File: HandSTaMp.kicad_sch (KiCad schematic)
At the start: 19 parts, among them J1 USB_C_Receptacle_USB2.0_16P, J2 SDI, J3 Pins, J4 ⏚, SW1 Row 0, Col+0, SW2 Row 0, Col+1, U2 PRTR5V0U2X, U4 CH32X035G8U6

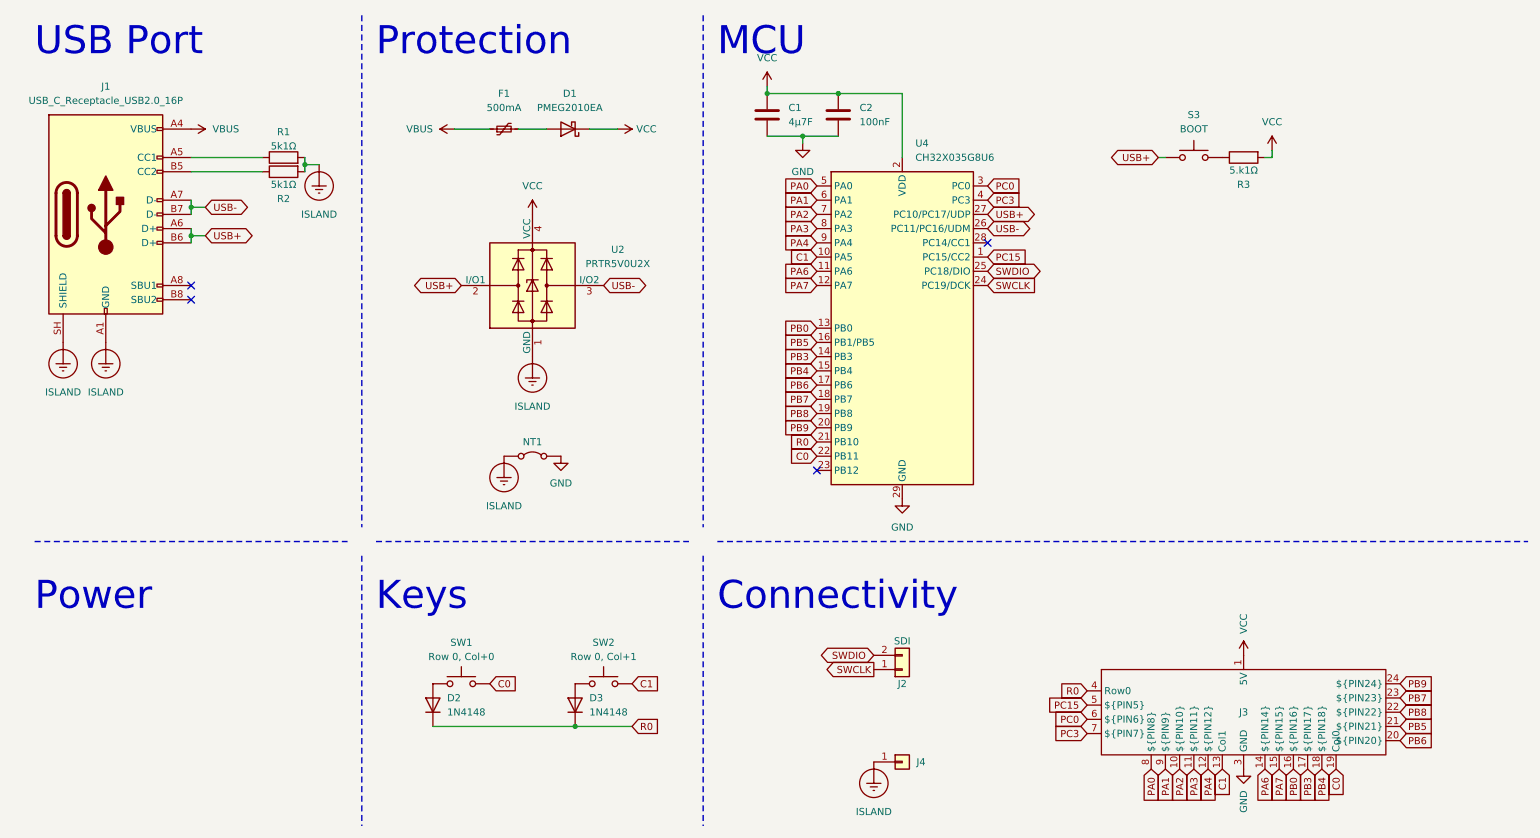
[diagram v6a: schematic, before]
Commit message: Draft equal number of extra corner pins on each side
Pins need relabelling!
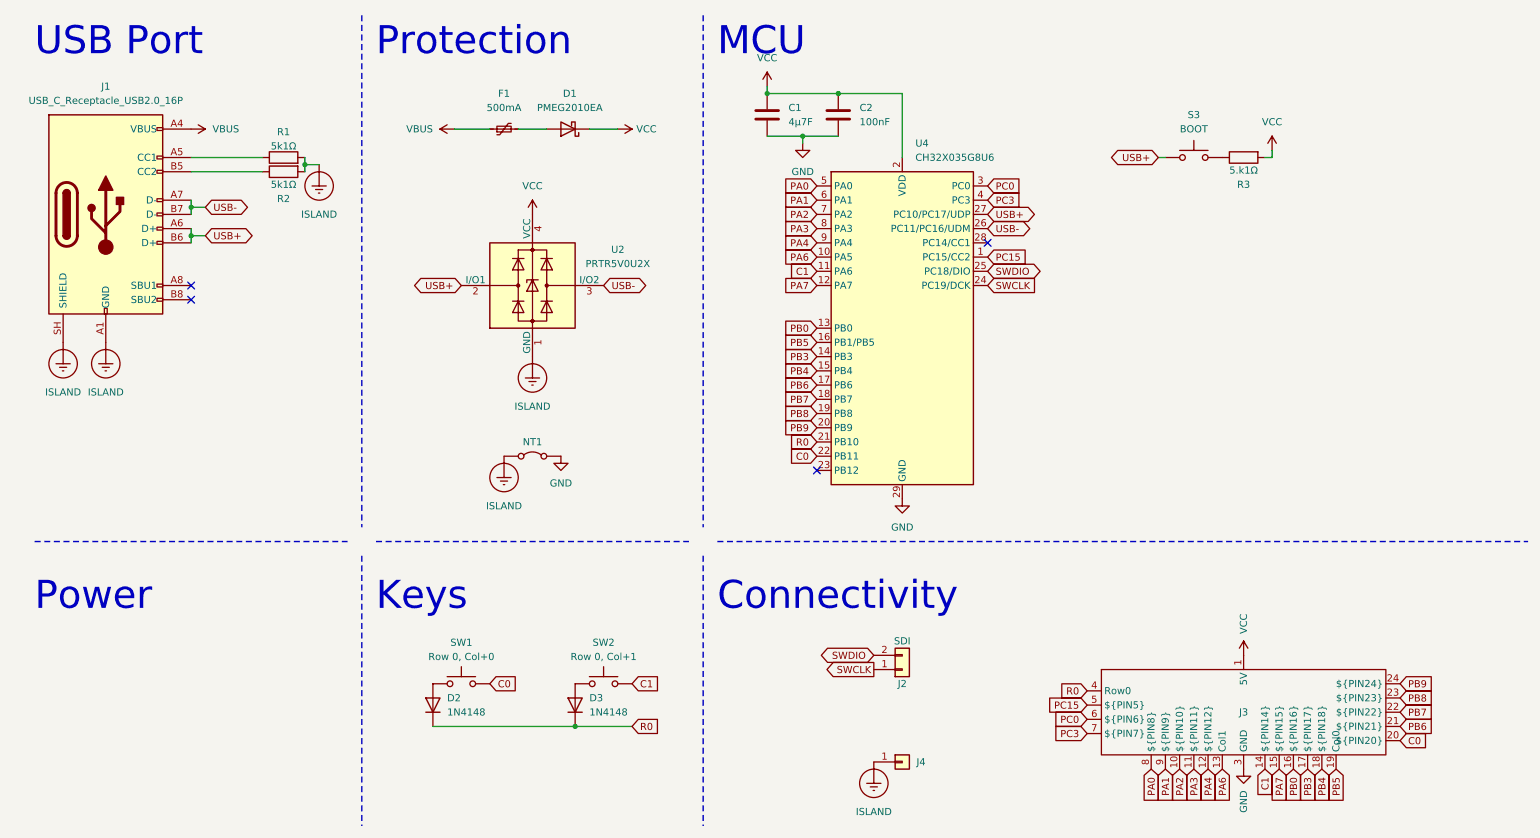
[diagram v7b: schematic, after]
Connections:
- net C0: now also J3.20 (${PIN20}); no longer J3.19 (Col0)
- net C1: now also J3.14 (${PIN14}), U4.11 (PA6); no longer J3.13 (Col1), U4.10 (PA5)
- net PA6: now also J3.13 (Col1), U4.10 (PA5); no longer J3.14 (${PIN14}), U4.11 (PA6)
- net PB5: now also J3.19 (Col0); no longer J3.21 (${PIN21})
- net PB6: now also J3.21 (${PIN21}); no longer J3.20 (${PIN20})
- net PB7: now also J3.22 (${PIN22}); no longer J3.23 (${PIN23})
- net PB8: now also J3.23 (${PIN23}); no longer J3.22 (${PIN22})
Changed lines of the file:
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@@
 	(global_label "PA6"
 		(shape input)
-		(at 154.94 60.96 180)
-		(fields_autoplaced yes)
-		(effects
-			(font
-				(size 1.27 1.27)
-			)
-			(justify right)
-		)
-		(property "Intersheetrefs" "${INTERSHEET_REFS}"
-			(at 149.2739 60.96 0)
+		(at 154.94 58.42 180)
+		(fields_autoplaced yes)
+		(effects
+			(font
+				(size 1.27 1.27)
+			)
+			(justify right)
+		)
+		(property "Intersheetrefs" "${INTERSHEET_REFS}"
+			(at 149.2739 58.42 0)
 			(hide yes)
 			(show_name no)
@@
 	(global_label "PB8"
 		(shape input)
-		(at 259.08 139.7 0)
-		(fields_autoplaced yes)
-		(effects
-			(font
-				(size 1.27 1.27)
-			)
-			(justify left)
-		)
-		(property "Intersheetrefs" "${INTERSHEET_REFS}"
-			(at 264.9893 139.7 0)
+		(at 259.08 137.16 0)
+		(fields_autoplaced yes)
+		(effects
+			(font
+				(size 1.27 1.27)
+			)
+			(justify left)
+		)
+		(property "Intersheetrefs" "${INTERSHEET_REFS}"
+			(at 264.9893 137.16 0)
 			(hide yes)
 			(show_name no)
@@
 		)
 	)
-	(global_label "C0"
+	(global_label "PB5"
 		(shape input)
 		(at 247.65 149.86 270)
@@
 		)
 		(property "Intersheetrefs" "${INTERSHEET_REFS}"
-			(at 247.65 155.3247 90)
+			(at 247.65 155.6862 90)
 			(hide yes)
 			(show_name no)
@@
 		)
 	)
-	(global_label "PB6"
+	(global_label "C0"
 		(shape input)
 		(at 259.08 144.78 0)
@@
 		)
 		(property "Intersheetrefs" "${INTERSHEET_REFS}"
-			(at 264.9595 144.78 0)
+			(at 263.8354 144.78 0)
 			(hide yes)
 			(show_name no)
@@
 	(global_label "PB7"
 		(shape input)
-		(at 259.08 137.16 0)
-		(fields_autoplaced yes)
-		(effects
-			(font
-				(size 1.27 1.27)
-			)
-			(justify left)
-		)
-		(property "Intersheetrefs" "${INTERSHEET_REFS}"
-			(at 264.7933 137.16 0)
+		(at 259.08 139.7 0)
+		(fields_autoplaced yes)
+		(effects
+			(font
+				(size 1.27 1.27)
+			)
+			(justify left)
+		)
+		(property "Intersheetrefs" "${INTERSHEET_REFS}"
+			(at 264.7933 139.7 0)
 			(hide yes)
 			(show_name no)
@@
 		)
 	)
-	(global_label "PB5"
+	(global_label "PB6"
 		(shape input)
 		(at 259.08 142.24 0)
@@
 		)
 		(property "Intersheetrefs" "${INTERSHEET_REFS}"
-			(at 264.9062 142.24 0)
+			(at 264.9595 142.24 0)
 			(hide yes)
 			(show_name no)
@@
 	(global_label "PA6"
 		(shape input)
-		(at 234.95 149.86 270)
-		(fields_autoplaced yes)
-		(effects
-			(font
-				(size 1.27 1.27)
-			)
-			(justify right)
-		)
-		(property "Intersheetrefs" "${INTERSHEET_REFS}"
-			(at 234.95 155.5261 90)
+		(at 227.33 149.86 270)
+		(fields_autoplaced yes)
+		(effects
+			(font
+				(size 1.27 1.27)
+			)
+			(justify right)
+		)
+		(property "Intersheetrefs" "${INTERSHEET_REFS}"
+			(at 227.33 155.5261 90)
 			(hide yes)
 			(show_name no)
@@
 	(global_label "C1"
 		(shape input)
-		(at 154.94 58.42 180)
-		(fields_autoplaced yes)
-		(effects
-			(font
-				(size 1.27 1.27)
-			)
-			(justify right)
-		)
-		(property "Intersheetrefs" "${INTERSHEET_REFS}"
-			(at 150.4042 58.42 0)
+		(at 154.94 60.96 180)
+		(fields_autoplaced yes)
+		(effects
+			(font
+				(size 1.27 1.27)
+			)
+			(justify right)
+		)
+		(property "Intersheetrefs" "${INTERSHEET_REFS}"
+			(at 150.4042 60.96 0)
 			(hide yes)
 			(show_name no)
@@
 	(global_label "C1"
 		(shape input)
-		(at 227.33 149.86 270)
-		(fields_autoplaced yes)
-		(effects
-			(font
-				(size 1.27 1.27)
-			)
-			(justify right)
-		)
-		(property "Intersheetrefs" "${INTERSHEET_REFS}"
-			(at 227.33 155.3247 90)
-			(hide yes)
-			(show_name no)
+		(at 234.95 149.86 270)
+		(fields_autoplaced yes)
+		(effects
+			(font
+				(size 1.27 1.27)
+			)
+			(justify right)
+		)
+		(property "Intersheetrefs" "${INTERSHEET_REFS}"
+			(at 234.95 155.3247 90)
+			(hide yes)
+			(show_name no)

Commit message: Fix pin assignments and labels
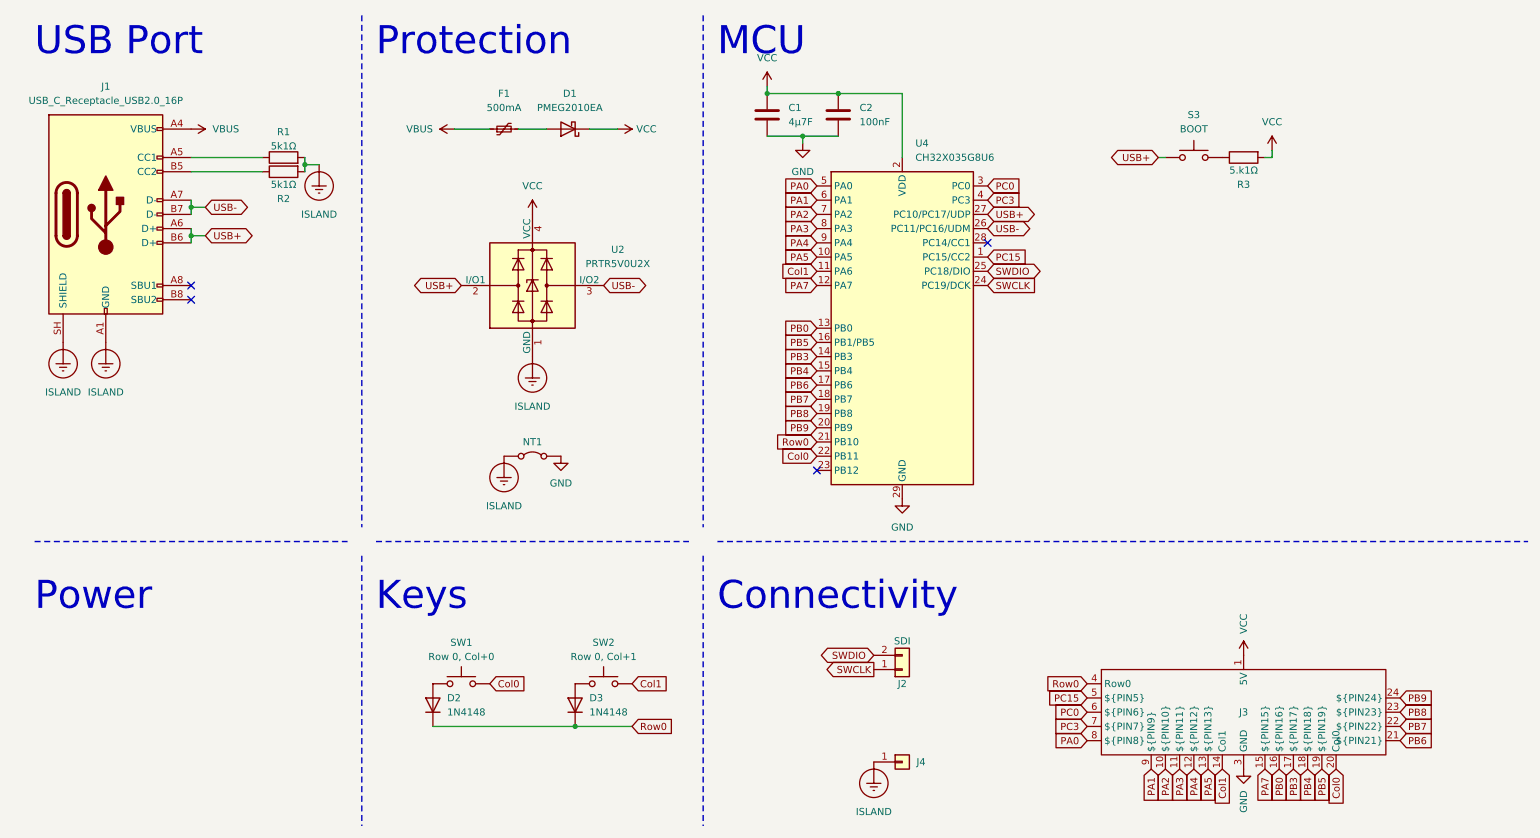
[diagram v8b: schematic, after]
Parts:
- J3: PIN13 (none) -> A5; PIN14 A6 -> (none); PIN19 (none) -> B5; PIN20 B6 -> (none); PIN21 B5 -> B6; PIN22 B8 -> B7; PIN23 B7 -> B8
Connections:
- net C0 renamed Col0
- net C1 renamed Col1
- net PA6 renamed PA5
- net R0 renamed Row0
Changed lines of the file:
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@@
 	(global_label "PB9"
 		(shape input)
-		(at 259.08 134.62 0)
+		(at 259.08 137.16 0)
 		(fields_autoplaced yes)
 		(effects
@@
 		)
 		(property "Intersheetrefs" "${INTERSHEET_REFS}"
-			(at 264.9484 134.62 0)
+			(at 264.9484 137.16 0)
 			(hide yes)
 			(show_name no)
@@
 		)
 	)
-	(global_label "C0"
+	(global_label "Col0"
 		(shape input)
 		(at 96.52 134.62 0)
@@
 		)
 		(property "Intersheetrefs" "${INTERSHEET_REFS}"
-			(at 101.9847 134.62 0)
+			(at 102.8536 134.62 0)
 			(hide yes)
 			(show_name no)
@@
 		)
 	)
-	(global_label "C1"
+	(global_label "Col1"
 		(shape input)
 		(at 121.92 134.62 0)
@@
 		)
 		(property "Intersheetrefs" "${INTERSHEET_REFS}"
-			(at 127.3847 134.62 0)
+			(at 128.034 134.62 0)
 			(hide yes)
 			(show_name no)
@@
 	(global_label "PA1"
 		(shape input)
-		(at 217.17 149.86 270)
+		(at 214.63 149.86 270)
 		(fields_autoplaced yes)
 		(effects
@@
 		)
 		(property "Intersheetrefs" "${INTERSHEET_REFS}"
-			(at 217.17 155.2767 90)
+			(at 214.63 155.2767 90)
 			(hide yes)
 			(show_name no)
@@
 		)
 	)
-	(global_label "PA6"
+	(global_label "PA5"
 		(shape input)
 		(at 154.94 58.42 180)
@@
 		)
 		(property "Intersheetrefs" "${INTERSHEET_REFS}"
-			(at 149.2739 58.42 0)
+			(at 149.2913 58.42 0)
 			(hide yes)
 			(show_name no)
@@
 	(global_label "PB8"
 		(shape input)
-		(at 259.08 137.16 0)
+		(at 259.08 139.7 0)
 		(fields_autoplaced yes)
 		(effects
@@
 		)
 		(property "Intersheetrefs" "${INTERSHEET_REFS}"
-			(at 264.9893 137.16 0)
+			(at 264.9893 139.7 0)
 			(hide yes)
 			(show_name no)
@@
 	(global_label "PC15"
 		(shape input)
-		(at 203.2 138.43 180)
+		(at 203.2 137.16 180)
 		(fields_autoplaced yes)
 		(effects
@@
 		)
 		(property "Intersheetrefs" "${INTERSHEET_REFS}"
-			(at 196.6902 138.43 0)
+			(at 196.6902 137.16 0)
 			(hide yes)
 			(show_name no)
@@
 	(global_label "PC0"
 		(shape input)
-		(at 203.2 140.97 180)
+		(at 203.2 139.7 180)
 		(fields_autoplaced yes)
 		(effects
@@
 		)
 		(property "Intersheetrefs" "${INTERSHEET_REFS}"
-			(at 197.3949 140.97 0)
+			(at 197.3949 139.7 0)
 			(hide yes)
 			(show_name no)
@@
 	(global_label "PB5"
 		(shape input)
-		(at 247.65 149.86 270)
+		(at 245.11 149.86 270)
 		(fields_autoplaced yes)
 		(effects
@@
 		)
 		(property "Intersheetrefs" "${INTERSHEET_REFS}"
-			(at 247.65 155.6862 90)
+			(at 245.11 155.6862 90)
 			(hide yes)
 			(show_name no)
@@
 		)
 	)
-	(global_label "C0"
+	(global_label "Col0"
 		(shape input)
-		(at 259.08 144.78 0)
+		(at 247.65 149.86 270)
 		(fields_autoplaced yes)
 		(effects
@@
 				(size 1.27 1.27)
 			)
-			(justify left)
+			(justify right)
 		)
 		(property "Intersheetrefs" "${INTERSHEET_REFS}"
-			(at 263.8354 144.78 0)
+			(at 247.65 156.1936 90)
 			(hide yes)
 			(show_name no)
@@
 					(size 1.27 1.27)
 				)
-				(justify left)
+				(justify right)
 			)
 		)
@@
 	(global_label "PB7"
 		(shape input)
-		(at 259.08 139.7 0)
+		(at 259.08 142.24 0)
 		(fields_autoplaced yes)
 		(effects
@@
 		)
 		(property "Intersheetrefs" "${INTERSHEET_REFS}"
-			(at 264.7933 139.7 0)
+			(at 264.7933 142.24 0)
 			(hide yes)
 			(show_name no)
@@
 	(global_label "PA0"
 		(shape input)
-		(at 214.63 149.86 270)
+		(at 203.2 144.78 180)
 		(fields_autoplaced yes)
 		(effects
@@
 		)
 		(property "Intersheetrefs" "${INTERSHEET_REFS}"
-			(at 214.63 155.603 90)
+			(at 197.457 144.78 0)
 			(hide yes)
 			(show_name no)
@@
 		)
 	)
-	(global_label "R0"
+	(global_label "Row0"
 		(shape input)
 		(at 121.92 142.24 0)
@@
 		)
 		(property "Intersheetrefs" "${INTERSHEET_REFS}"
-			(at 127.3847 142.24 0)
+			(at 129.0936 142.24 0)
 			(hide yes)
 			(show_name no)
@@
 	(global_label "PA7"
 		(shape input)
-		(at 237.49 149.86 270)
+		(at 234.95 149.86 270)
 		(fields_autoplaced yes)
 		(effects
@@
 		)
 		(property "Intersheetrefs" "${INTERSHEET_REFS}"
-			(at 237.49 155.3599 90)
+			(at 234.95 155.3599 90)
 			(hide yes)
 			(show_name no)
@@
 	(global_label "PB3"
 		(shape input)
-		(at 242.57 149.86 270)
+		(at 240.03 149.86 270)
 		(fields_autoplaced yes)
 		(effects
@@
 		)
 		(property "Intersheetrefs" "${INTERSHEET_REFS}"
-			(at 242.57 155.6676 90)
+			(at 240.03 155.6676 90)
 			(hide yes)
 			(show_name no)
@@
 	(global_label "PB6"
 		(shape input)
-		(at 259.08 142.24 0)
+		(at 259.08 144.78 0)
 		(fields_autoplaced yes)
 		(effects
@@
 		)
 		(property "Intersheetrefs" "${INTERSHEET_REFS}"
-			(at 264.9595 142.24 0)
+			(at 264.9595 144.78 0)
 			(hide yes)
 			(show_name no)
@@
 		)
 	)
-	(global_label "PA6"
+	(global_label "PA5"
 		(shape input)
-		(at 227.33 149.86 270)
+		(at 224.79 149.86 270)
 		(fields_autoplaced yes)
 		(effects
@@
 		)
 		(property "Intersheetrefs" "${INTERSHEET_REFS}"
-			(at 227.33 155.5261 90)
+			(at 224.79 155.5087 90)
 			(hide yes)
 			(show_name no)
@@
 		)
 	)
-	(global_label "R0"
+	(global_label "Row0"
 		(shape input)
-		(at 203.2 135.89 180)
+		(at 203.2 134.62 180)
 		(fields_autoplaced yes)
 		(effects
@@
 		)
 		(property "Intersheetrefs" "${INTERSHEET_REFS}"
-			(at 197.7353 135.89 0)
+			(at 196.0264 134.62 0)
 			(hide yes)
 			(show_name no)
@@
 		)
 	)
-	(global_label "C1"
+	(global_label "Col1"
 		(shape input)
 		(at 154.94 60.96 180)
@@
 		)
 		(property "Intersheetrefs" "${INTERSHEET_REFS}"
-			(at 150.4042 60.96 0)
+			(at 148.826 60.96 0)
 			(hide yes)
 			(show_name no)
@@
 		)
 	)
-	(global_label "C1"
+	(global_label "Col1"
 		(shape input)
-		(at 234.95 149.86 270)
+		(at 227.33 149.86 270)
 		(fields_autoplaced yes)
 		(effects
@@
 		)
 		(property "Intersheetrefs" "${INTERSHEET_REFS}"
-			(at 234.95 155.3247 90)
+			(at 227.33 155.974 90)
 			(hide yes)
 			(show_name no)
@@
 	(global_label "PB4"
 		(shape input)
-		(at 245.11 149.86 270)
+		(at 242.57 149.86 270)
 		(fields_autoplaced yes)
 		(effects
@@
 		)
 		(property "Intersheetrefs" "${INTERSHEET_REFS}"
-			(at 245.11 155.7395 90)
+			(at 242.57 155.7395 90)
 			(hide yes)
 			(show_name no)
@@
 	(global_label "PA4"
 		(shape input)
-		(at 224.79 149.86 270)
+		(at 222.25 149.86 270)
 		(fields_autoplaced yes)
 		(effects
@@
 		)
 		(property "Intersheetrefs" "${INTERSHEET_REFS}"
-			(at 224.79 155.5261 90)
+			(at 222.25 155.5261 90)
 			(hide yes)
 			(show_name no)
@@
 		)
 	)
-	(global_label "R0"
+	(global_label "Row0"
 		(shape input)
 		(at 154.94 91.44 180)
@@
 		)
 		(property "Intersheetrefs" "${INTERSHEET_REFS}"
-			(at 150.0729 91.44 0)
+			(at 147.7664 91.44 0)
 			(hide yes)
 			(show_name no)
@@
 	(global_label "PA2"
 		(shape input)
-		(at 219.71 149.86 270)
+		(at 217.17 149.86 270)
 		(fields_autoplaced yes)
 		(effects
@@
 		)
 		(property "Intersheetrefs" "${INTERSHEET_REFS}"
-			(at 219.71 155.4852 90)
+			(at 217.17 155.4852 90)
 			(hide yes)
 			(show_name no)
@@
 	(global_label "PC3"
 		(shape input)
-		(at 203.2 143.51 180)
+		(at 203.2 142.24 180)
 		(fields_autoplaced yes)
 		(effects
@@
 		)
 		(property "Intersheetrefs" "${INTERSHEET_REFS}"
-			(at 197.4731 143.51 0)
+			(at 197.4731 142.24 0)
 			(hide yes)
 			(show_name no)
@@
 	(global_label "PB0"
 		(shape input)
-		(at 240.03 149.86 270)
+		(at 237.49 149.86 270)
 		(fields_autoplaced yes)
 		(effects
@@
 		)
 		(property "Intersheetrefs" "${INTERSHEET_REFS}"
-			(at 240.03 155.7805 90)
+			(at 237.49 155.7805 90)
 			(hide yes)
 			(show_name no)
@@
 	(global_label "PA3"
 		(shape input)
-		(at 222.25 149.86 270)
+		(at 219.71 149.86 270)
 		(fields_autoplaced yes)
 		(effects
@@
 		)
 		(property "Intersheetrefs" "${INTERSHEET_REFS}"
-			(at 222.25 155.4901 90)
+			(at 219.71 155.4901 90)
 			(hide yes)
 			(show_name no)
@@
 		)
 	)
-	(global_label "C0"
+	(global_label "Col0"
 		(shape input)
 		(at 154.94 93.98 180)
@@
 		)
 		(property "Intersheetrefs" "${INTERSHEET_REFS}"
-			(at 150.1846 93.98 0)
+			(at 148.6064 93.98 0)
 			(hide yes)
 			(show_name no)
@@
 			)
 		)
-		(property "PIN14" "A6"
+		(property "PIN13" "A5"
 			(at 231.14 139.7 0)
 			(hide yes)
@@
 			)
 		)
-		(property "PIN20" "B6"
+		(property "PIN19" "B5"
 			(at 231.14 139.7 0)
 			(hide yes)
@@
 			)
 		)
-		(property "PIN21" "B5"
+		(property "PIN21" "B6"
 			(at 231.14 139.7 0)
 			(hide yes)
@@
 			)
 		)
-		(property "PIN22" "B8"
+		(property "PIN22" "B7"
 			(at 231.14 139.7 0)
 			(hide yes)
@@
 			)
 		)
-		(property "PIN23" "B7"
+		(property "PIN23" "B8"
 			(at 231.14 139.7 0)
 			(hide yes)
